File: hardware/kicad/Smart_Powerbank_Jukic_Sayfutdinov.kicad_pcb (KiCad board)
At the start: 4 copper layers, 83 x 26 mm, 89 parts, among them J1 USB_C_Receptacle_USB2.0_16P, J2 USB_C_Receptacle_USB2.0_16P, J3 Conn_01x04_Pin, J4 USB_C_Receptacle_USB2.0_16P, J5 Conn_01x04_Pin, J6 Conn_01x03_Pin, J7 Conn_01x04_Pin, SW1 SW_Push, SW2 SW_Push, U1 ATmega328-A, U2 AP2112K-3.3, U3 INA219AxD, U4 INA219AxD, U5 BQ27441-G1, U6 BQ24074RGT, U7 MT3608, U8 ESP-12E

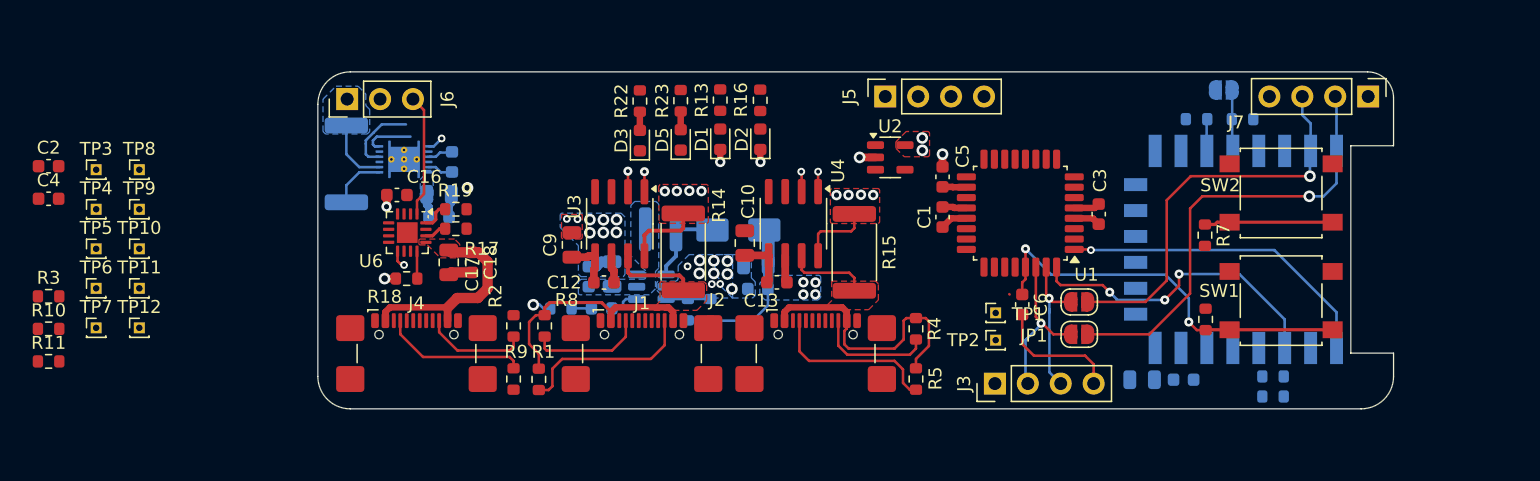
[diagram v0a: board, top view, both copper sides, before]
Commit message: Finished component placement, i2c routing and uart routing
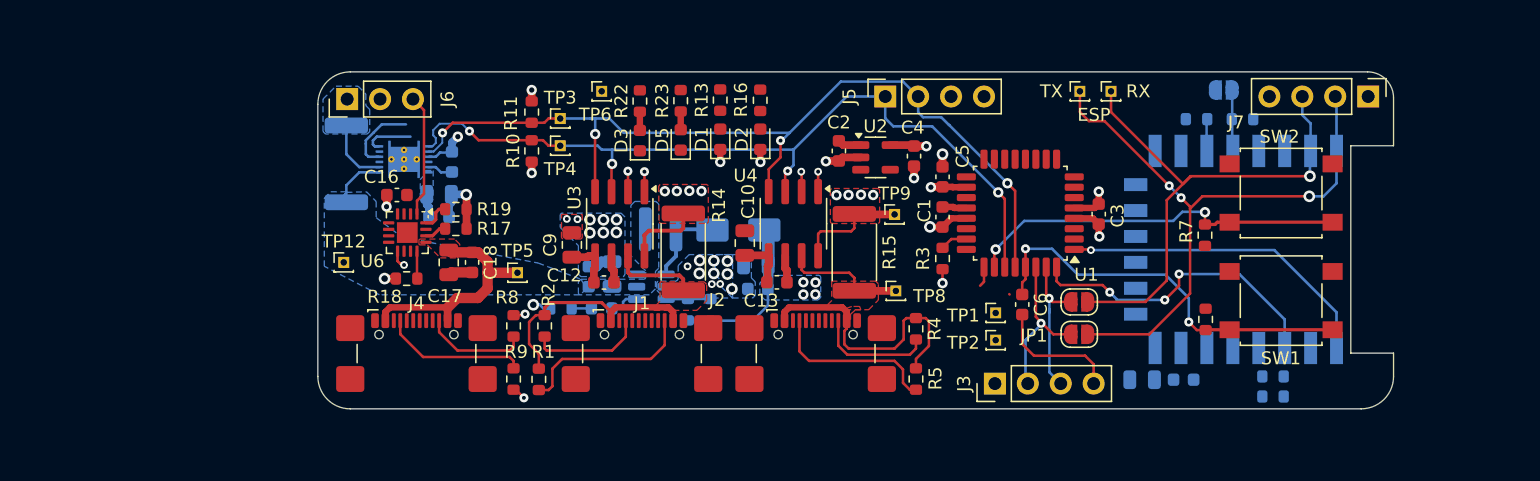
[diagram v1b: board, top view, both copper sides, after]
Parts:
- removed TP7: TestPoint_Probe, Connector_PinHeader_1.00mm:PinHeader_1x01_P1.00mm_Vertical
- moved RX 76.0 mm to (167.2, 94.5)
- moved TX 74.1 mm to (164.8, 94.5)
- moved R3 69.0 mm to (154.2, 107.4), turned to -90 degrees
- moved C4 66.9 mm to (152.0, 99.5), turned to -90 degrees
- moved C2 61.0 mm to (146.2, 99.1), turned to -90 degrees
- moved TP8 59.1 mm to (150.6, 109.9)
- moved TP9 58.3 mm to (150.5, 104.0)
- moved R11 41.9 mm to (122.5, 96.1), turned to -90 degrees
- moved TP6 41.9 mm to (127.9, 94.5)
- moved R10 39.7 mm to (122.5, 99.1), turned to 90 degrees
- moved TP4 36.1 mm to (124.7, 98.7)
- moved TP3 36.0 mm to (124.7, 96.6)
- moved TP5 32.6 mm to (121.4, 108.5)
- moved TP12 16.6 mm to (108.0, 107.7)
- moved U2 1.13 mm to (149.0, 99.6)
- renumbered TP10 to RX, TP11 to TX
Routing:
- net /SCL: track 0.00 -> 70.3 mm, vias 0 -> 4
- net /SDA: track 1.25 -> 64.9 mm, vias 1 -> 4
- net /SW_MODE: track 10.1 -> 29.8 mm, vias 0 -> 2
- net /TX_ESP: track 34.6 -> 47.9 mm, vias 1 -> 3
- net GND: track 28.0 -> 39.6 mm, vias 28 -> 35
- net /RX_ESP: track 31.5 -> 41.8 mm
- net +3.3V: track 13.4 -> 20.9 mm, vias 3 -> 7
- net +5V: track 22.7 -> 25.8 mm
- net VOUT2: track 27.3 -> 30.4 mm
- net VIN_USB: track 15.8 -> 18.0 mm
- net /TS: track 9.44 -> 11.6 mm
- net VCC: track 4.81 -> 6.64 mm
- net /GPOUT: track 3.89 -> 5.45 mm
- net (no net): vias 1 -> 0
- added copper zone on F.Cu, net VOUT1
- removed copper zone on F.Cu, net +3.3V
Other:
- board text added: "ESP"

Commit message: finished atmega logic pin routing and revised power layout
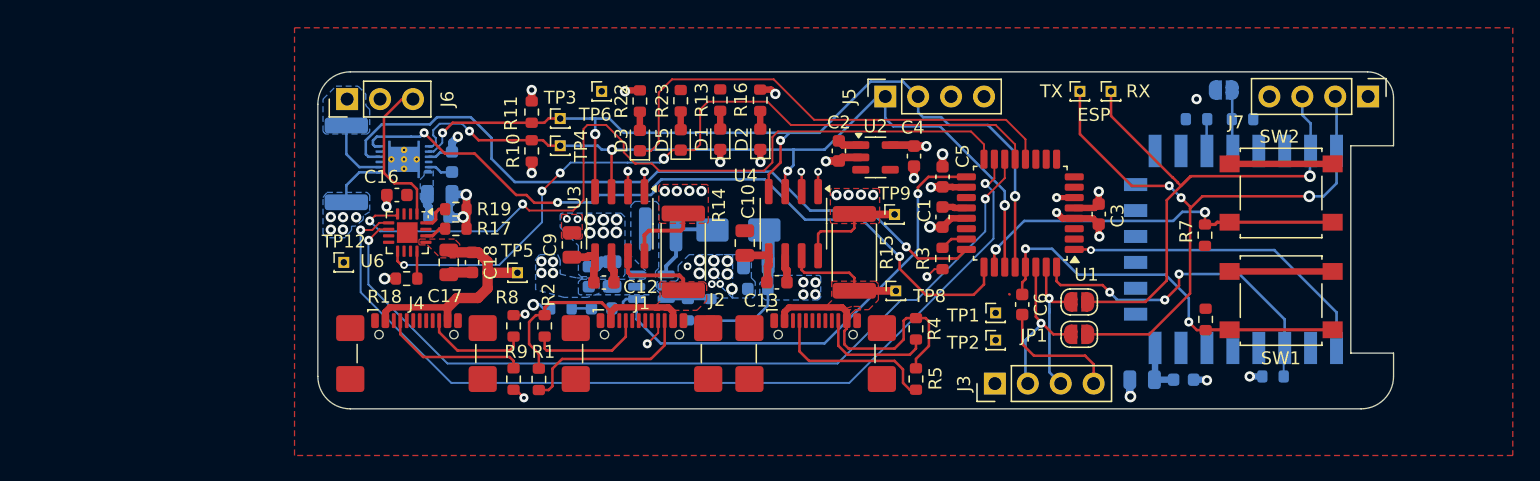
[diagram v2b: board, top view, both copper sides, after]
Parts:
- removed R34: 10k, Resistor_SMD:R_0603_1608Metric
- moved C7 0.05 mm to (115.4, 102.5)
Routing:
- net /EN2: track 0.00 -> 70.4 mm, vias 0 -> 2
- net /EN1: track 0.00 -> 65.9 mm, vias 0 -> 2
- net /CE: track 0.00 -> 63.1 mm, vias 0 -> 2
- net /CHG: track 1.39 -> 59.2 mm, vias 1 -> 4
- net /GPOUT: track 5.45 -> 57.4 mm, vias 0 -> 3
- net /BIN: track 5.81 -> 55.7 mm, vias 0 -> 1
- net /PGOOD: track 0.00 -> 37.8 mm
- net /EN_OUT: track 2.01 -> 37.9 mm, vias 0 -> 1
- net GND: track 39.6 -> 62.0 mm, vias 35 -> 41
- net +3.3V: track 20.9 -> 29.3 mm, vias 7 -> 10
- net /TS: track 11.6 -> 14.2 mm
- net /ESP_EN: track 24.3 -> 26.6 mm
- net /SCL: track 70.3 -> 72.1 mm
- net Net-(D1-A): track 0.00 -> 1.41 mm
- net Net-(D2-A): track 0.00 -> 1.40 mm
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- added copper zone on In1.Cu, net VCC

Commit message: cleanup and prep for ordering
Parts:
- moved J7 0.26 mm to (186.8, 95.0)
- moved C21 0.08 mm to (139.8, 108.0)
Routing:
- net /TX: track 11.7 -> 16.1 mm
- net /RX: track 12.5 -> 14.8 mm
- net GND: vias 41 -> 40
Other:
- outline, holes or cut-outs redrawn
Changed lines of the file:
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@@
 	(footprint "Connector_PinHeader_2.54mm:PinHeader_1x04_P2.54mm_Vertical"
 		(layer "F.Cu")
-		(at 187.04 94.9 -90)
+		(at 186.8 95 -90)
 		(descr "Through hole straight pin header, 1x04, 2.54mm pitch, single row")
 		(tags "Through hole pin header THT 1x04 2.54mm single row")
@@
 	(footprint "Capacitor_SMD:C_0805_2012Metric"
 		(layer "B.Cu")
-		(at 139.8 107.9 180)
+		(at 139.79795 107.977325 180)
 		(descr "Capacitor SMD 0805 (2012 Metric), square (rectangular) end terminal, IPC-7351 nominal, (Body size source: IPC-SM-782 page 76, https://www.pcb-3d.com/wordpress/wp-content/uploads/ipc-sm-782a_amendment_1_and_2.pdf, https://docs.google.com/spreadsheets/d/1BsfQQcO9C6DZCsRaXUlFlo91Tg2WpOkGARC1WS5S8t0/edit?usp=sharing), generated with kicad-footprint-generator")
 		(tags "capacitor")
@@
 	)
 	(gr_line
-		(start 189 98.7)
+		(start 189 98.45)
 		(end 189 95)
 		(stroke
@@
 	)
 	(gr_line
-		(start 189 114.7)
-		(end 185.7 114.7)
+		(start 189 114.95)
+		(end 185.7 114.95)
 		(stroke
 			(width 0.05)
@@
 	)
 	(gr_line
-		(start 185.7 114.7)
-		(end 185.7 98.7)
+		(start 185.7 114.95)
+		(end 185.7 98.45)
 		(stroke
 			(width 0.05)
@@
 	(gr_line
 		(start 189 116.5)
-		(end 189 114.7)
+		(end 189 114.95)
 		(stroke
 			(width 0.05)
@@
 	)
 	(gr_line
-		(start 185.7 98.7)
-		(end 189 98.7)
+		(start 185.7 98.45)
+		(end 189 98.45)
 		(stroke
 			(width 0.05)
@@
 	)
 	(via
-		(at 137.603079 107.598099)
-		(size 0.9)
-		(drill 0.5)
-		(layers "F.Cu" "B.Cu")
-		(free yes)
-		(net 2)
-	)
-	(via
 		(at 137.05 99.95)
 		(size 0.8)
@@
 	)
 	(segment
-		(start 159.375 110.175)
-		(end 159.35 110.15)
-		(width 0.2)
-		(layer "F.Cu")
-		(net 4)
-	)
-	(segment
 		(start 174.5 112.925)
 		(end 174.525 112.9)
@@
 	)
 	(segment
-		(start 162.45 110.5)
-		(end 162.425 110.475)
+		(start 162.425 110.475)
+		(end 162.45 110.5)
 		(width 0.2)
 		(layer "B.Cu")
@@
 	)
 	(segment
-		(start 162.45 111.35)
-		(end 162.45 110.5)
+		(start 162.45 110.5)
+		(end 162.45 116.18)
 		(width 0.2)
 		(layer "B.Cu")
@@
 	)
 	(segment
-		(start 163.32 117.05)
-		(end 162.45 116.18)
+		(start 158.3 111.6)
+		(end 161.3 111.6)
 		(width 0.2)
 		(layer "B.Cu")
@@
 	)
 	(segment
-		(start 162.45 111.35)
-		(end 162.45 111.55)
+		(start 161.3 111.6)
+		(end 162.425 110.475)
 		(width 0.2)
 		(layer "B.Cu")
@@
 	(segment
 		(start 162.45 116.18)
-		(end 162.45 111.35)
+		(end 163.32 117.05)
 		(width 0.2)
 		(layer "B.Cu")
@@
 	)
 	(segment
+		(start 158.3 113.7)
+		(end 160.6 113.7)
+		(width 0.2)
+		(layer "B.Cu")
+		(net 31)
+	)
+	(segment
 		(start 123.5 111.2)
 		(end 123.5 111.775)
@@
 	)
 	(segment
-		(start 115.989 111.169)
-		(end 116.01 111.19)
-		(width 0.5)
-		(layer "F.Cu")
-		(net 36)
-	)
-	(segment
 		(start 118.35 110.45)
 		(end 119.1 109.7)
@@
 			(clearance 0)
 		)
-		(min_thickness 0.25)
+		(min_thickness 0.1)
 		(filled_areas_thickness no)
-		(fill
+		(fill yes
 			(thermal_gap 0.5)
 			(thermal_bridge_width 0.5)
@@
 	)
 	(zone
+		(net 2)
+		(net_name "GND")
+		(layer "F.Cu")
+		(hatch edge 0.5)
+		(priority 17)
+		(connect_pads yes
+			(clearance 0)
+		)
+		(min_thickness 0.1)
+		(filled_areas_thickness no)
+		(fill yes
+			(thermal_gap 0.5)
+			(thermal_bridge_width 0.5)
+		)
+		(polygon
+			(pts
+				(xy 120.65 111.35) (xy 119.3 111.45) (xy 116.65 111.45) (xy 116.35 111.7) (xy 116.35 112.7) (xy 116.65 112.95)
+				(xy 117.25 112.95) (xy 117.5 113.15) (xy 117.5 113.65) (xy 117.8 113.95) (xy 119.65 113.95) (xy 120 113.6)
+				(xy 120 113.15) (xy 120.9 112.35) (xy 122 112.3) (xy 122.6 111.75) (xy 122.6 111.5) (xy 122.4 111.35)
+			)
+		)
+	)
+	(zone
 		(net 34)
 		(net_name "VOUT1")
@@
 	)
 	(zone
+		(net 2)
+		(net_name "GND")
+		(layer "F.Cu")
+		(hatch edge 0.5)
+		(priority 18)
+		(connect_pads yes
+			(clearance 0)
+		)
+		(min_thickness 0.1)
+		(filled_areas_thickness no)
+		(fill yes
+			(thermal_gap 0.5)
+			(thermal_bridge_width 0.5)
+		)
+		(polygon
+			(pts
+				(xy 151.05 111.15) (xy 149.5 111.15) (xy 147.5 111.35) (xy 147.1 111.55) (xy 147.1 112.65) (xy 147.4 112.85)
+				(xy 147.95 112.85) (xy 148.25 113.1) (xy 148.25 113.5) (xy 148.6 113.9) (xy 150.45 113.9) (xy 150.75 113.65)
+				(xy 150.8 112.2) (xy 151.4 111.7)
+			)
+		)
+	)
+	(zone
+		(net 2)
+		(net_name "GND")
+		(layer "B.Cu")
+		(hatch edge 0.5)
+		(connect_pads
+			(clearance 0)
+		)
+		(min_thickness 0.25)
+		(filled_areas_thickness no)
+		(fill yes
+			(thermal_gap 0.5)
+			(thermal_bridge_width 0.5)
+		)
+		(polygon
+			(pts
+				(xy 104.3 89.454301) (xy 198.3 89.454301) (xy 198.3 122.454301) (xy 104.3 122.454301)
+			)
+		)
+	)
+	(zone
 		(net 38)
 		(net_name "VCC")
@@
 			)
 		)
-	)
-	(zone
-		(net 2)
-		(net_name "GND")
-		(layer "In2.Cu")
-		(hatch edge 0.5)
-		(connect_pads
-			(clearance 0)
-		)
-		(min_thickness 0.25)
-		(filled_areas_thickness no)
-		(fill yes
-			(thermal_gap 0.5)
-			(thermal_bridge_width 0.5)
-		)
-		(polygon
-			(pts
-				(xy 90.3 88) (xy 184.3 88) (xy 184.3 121) (xy 90.3 121)
-			)
-		)
-	)
-	(zone
-		(net 2)
-		(net_name "GND")
-		(layer "In2.Cu")
-		(hatch edge 0.5)
-		(connect_pads
-			(clearance 0)
-		)
-		(min_thickness 0.25)
-		(filled_areas_thickness no)
-		(fill yes
-			(thermal_gap 0.5)
-			(thermal_bridge_width 0.5)
-		)
-		(polygon
-			(pts
-				(xy 109.9 90.4) (xy 203.9 90.4) (xy 203.9 123.4) (xy 109.9 123.4)
-			)
-		)

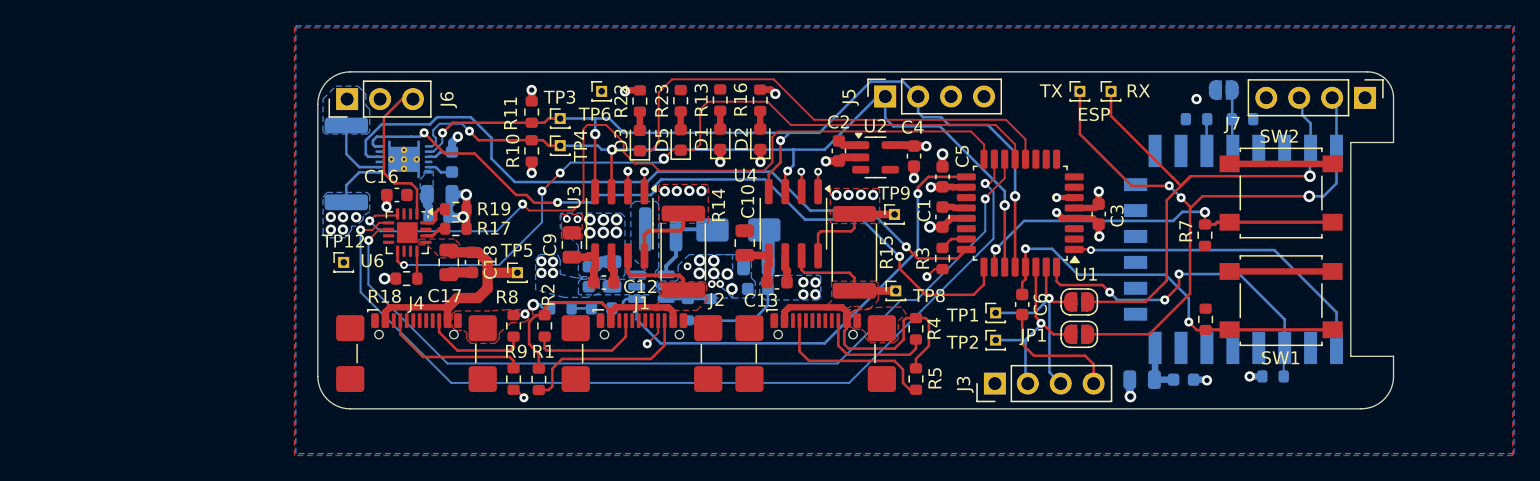
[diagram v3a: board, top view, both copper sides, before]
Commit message: Added mounting holes and fixed drc issues
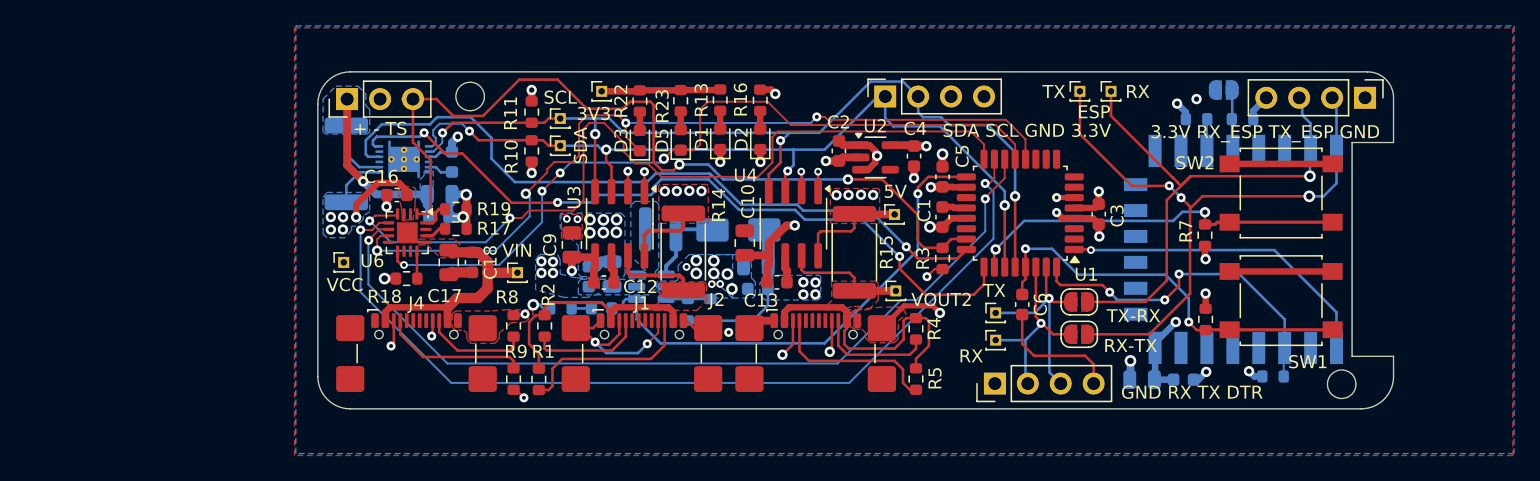
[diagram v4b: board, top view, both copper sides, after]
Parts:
- added ?: , , F.Cu at (185.0, 117.1)
- added ?: , , F.Cu at (117.8, 94.9)
- + - TS: renamed from J6
- 3.3V RX_ESP TX_ESP GND: renamed from J7
- GND RX TX DTR: renamed from J3
- SDA SCL GND 3.3V: renamed from J5
- renumbered TP6 to 3V3, TP9 to 5V, TP2 to RX, JP1 to RX-TX, TP3 to SCL, TP4 to SDA, TP1 to TX, JP2 to TX-RX, TP12 to VCC, TP5 to VIN, TP8 to VOUT2
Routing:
- net /TS: track 14.2 -> 65.8 mm, vias 0 -> 2
- net VCC: track 6.64 -> 51.0 mm, vias 9 -> 10
- net GND: track 62.0 -> 93.1 mm, vias 40 -> 47
- net /PGOOD: track 37.8 -> 65.1 mm, vias 0 -> 4
- net +3.3V: track 29.3 -> 50.3 mm, vias 10 -> 15
- net +5V: track 27.1 -> 39.3 mm
- net /BAT+: track 7.08 -> 19.3 mm, vias 0 -> 1
- net /CE: track 63.1 -> 63.8 mm
- added copper zone on F.Cu, net VCC
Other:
- outline, holes or cut-outs redrawn

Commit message: changed silkscreen labels and created gerbers
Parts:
- moved SDA SCL GND 3.3V 7.62 mm to (157.4, 94.9), turned to -90 degrees
- renumbered D2 to +5V, D1 to 3V3, D5 to CG, D3 to PG
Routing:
- net /SCL: track 72.1 -> 74.8 mm
- net /SDA: track 65.4 -> 67.7 mm
- net +3.3V: track 50.3 -> 50.9 mm

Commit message: made final changes; added gerbers.zip; orderd parts from inventory
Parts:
- 3.3V GND SCL SDA: renamed from SDA SCL GND 3.3V
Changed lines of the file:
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@@
 			(outputformat 1)
 			(mirror no)
-			(drillshape 1)
+			(drillshape 0)
 			(scaleselection 1)
-			(outputdirectory "")
+			(outputdirectory "../gerbers/")
 		)
 	)
@@
 		(descr "Through hole straight socket strip, 1x04, 2.54mm pitch, single row (from Kicad 4.0.7), script generated")
 		(tags "Through hole socket strip THT 1x04 2.54mm single row")
-		(property "Reference" "SDA SCL GND 3.3V"
-			(at -2.65 10.92 0)
+		(property "Reference" "3.3V GND SCL SDA"
+			(at 2.575 -2.9 0)
 			(layer "F.SilkS")
 			(effects
@@
 	)
 	(gr_text "ESP\n"
-		(at 164.6 96.7 0)
+		(at 167.55 96.95 0)
 		(layer "F.SilkS")
 		(effects
@@
 		)
 	)
+	(dimension
+		(type orthogonal)
+		(layer "Cmts.User")
+		(pts
+			(xy 106 116.5) (xy 139.94 119.55)
+		)
+		(height 11.95)
+		(orientation 0)
+		(format
+			(prefix "")
+			(suffix "")
+			(units 3)
+			(units_format 0)
+			(precision 4)
+			(suppress_zeroes yes)
+		)
+		(style
+			(thickness 0.1)
+			(arrow_length 1.27)
+			(text_position_mode 0)
+			(arrow_direction outward)
+			(extension_height 0.58642)
+			(extension_offset 0.5)
+			(keep_text_aligned yes)
+		)
+		(gr_text "33,94"
+			(at 122.97 127.3 0)
+			(layer "Cmts.User")
+			(effects
+				(font
+					(size 1 1)
+					(thickness 0.15)
+				)
+			)
+		)
+	)
+	(dimension
+		(type orthogonal)
+		(layer "Cmts.User")
+		(pts
+			(xy 106.01 113.7) (xy 109.15 116.75)
+		)
+		(height 9.95)
+		(orientation 0)
+		(format
+			(prefix "")
+			(suffix "")
+			(units 3)
+			(units_format 0)
+			(precision 4)
+			(suppress_zeroes yes)
+		)
+		(style
+			(thickness 0.1)
+			(arrow_length 1.27)
+			(text_position_mode 0)
+			(arrow_direction outward)
+			(extension_height 0.58642)
+			(extension_offset 0.5)
+			(keep_text_aligned yes)
+		)
+		(gr_text "3,14"
+			(at 107.58 122.5 0)
+			(layer "Cmts.User")
+			(effects
+				(font
+					(size 1 1)
+					(thickness 0.15)
+				)
+			)
+		)
+	)
+	(dimension
+		(type orthogonal)
+		(layer "Cmts.User")
+		(pts
+			(xy 106.01 115.85) (xy 126.55 118.9)
+		)
+		(height 9)
+		(orientation 0)
+		(format
+			(prefix "")
+			(suffix "")
+			(units 3)
+			(units_format 0)
+			(precision 4)
+			(suppress_zeroes yes)
+		)
+		(style
+			(thickness 0.1)
+			(arrow_length 1.27)
+			(text_position_mode 2)
+			(arrow_direction outward)
+			(extension_height 0.58642)
+			(extension_offset 0.5)
+			(keep_text_aligned yes)
+		)
+		(gr_text "20,54"
+			(at 115.9 125.1 0)
+			(layer "Cmts.User")
+			(effects
+				(font
+					(size 1 1)
+					(thickness 0.15)
+				)
+			)
+		)
+	)
+	(dimension
+		(type orthogonal)
+		(layer "Cmts.User")
+		(pts
+			(xy 106 95.5) (xy 193.22 98.58)
+		)
+		(height -8.05)
+		(orientation 0)
+		(format
+			(prefix "")
+			(suffix "")
+			(units 3)
+			(units_format 0)
+			(precision 4)
+			(suppress_zeroes yes)
+		)
+		(style
+			(thickness 0.1)
+			(arrow_length 1.27)
+			(text_position_mode 0)
+			(arrow_direction outward)
+			(extension_height 0.58642)
+			(extension_offset 0.5)
+			(keep_text_aligned yes)
+		)
+		(gr_text "87,22"
+			(at 149.61 86.3 0)
+			(layer "Cmts.User")
+			(effects
+				(font
+					(size 1 1)
+					(thickness 0.15)
+				)
+			)
+		)
+	)
+	(dimension
+		(type orthogonal)
+		(layer "Cmts.User")
+		(pts
+			(xy 108.64 119.13) (xy 108.5 93)
+		)
+		(height -7.14)
+		(orientation 1)
+		(format
+			(prefix "")
+			(suffix "")
+			(units 3)
+			(units_format 0)
+			(precision 4)
+			(suppress_zeroes yes)
+		)
+		(style
+			(thickness 0.1)
+			(arrow_length 1.27)
+			(text_position_mode 0)
+			(arrow_direction outward)
+			(extension_height 0.58642)
+			(extension_offset 0.5)
+			(keep_text_aligned yes)
+		)
+		(gr_text "26,13"
+			(at 100.35 106.065 90)
+			(layer "Cmts.User")
+			(effects
+				(font
+					(size 1 1)
+					(thickness 0.15)
+				)
+			)
+		)
+	)
